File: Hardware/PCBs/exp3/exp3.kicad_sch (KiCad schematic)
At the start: 8 parts, among them J1 Conn_01x07_Female, J2 Conn_01x06_Female, U1 74HC86, U2 7483

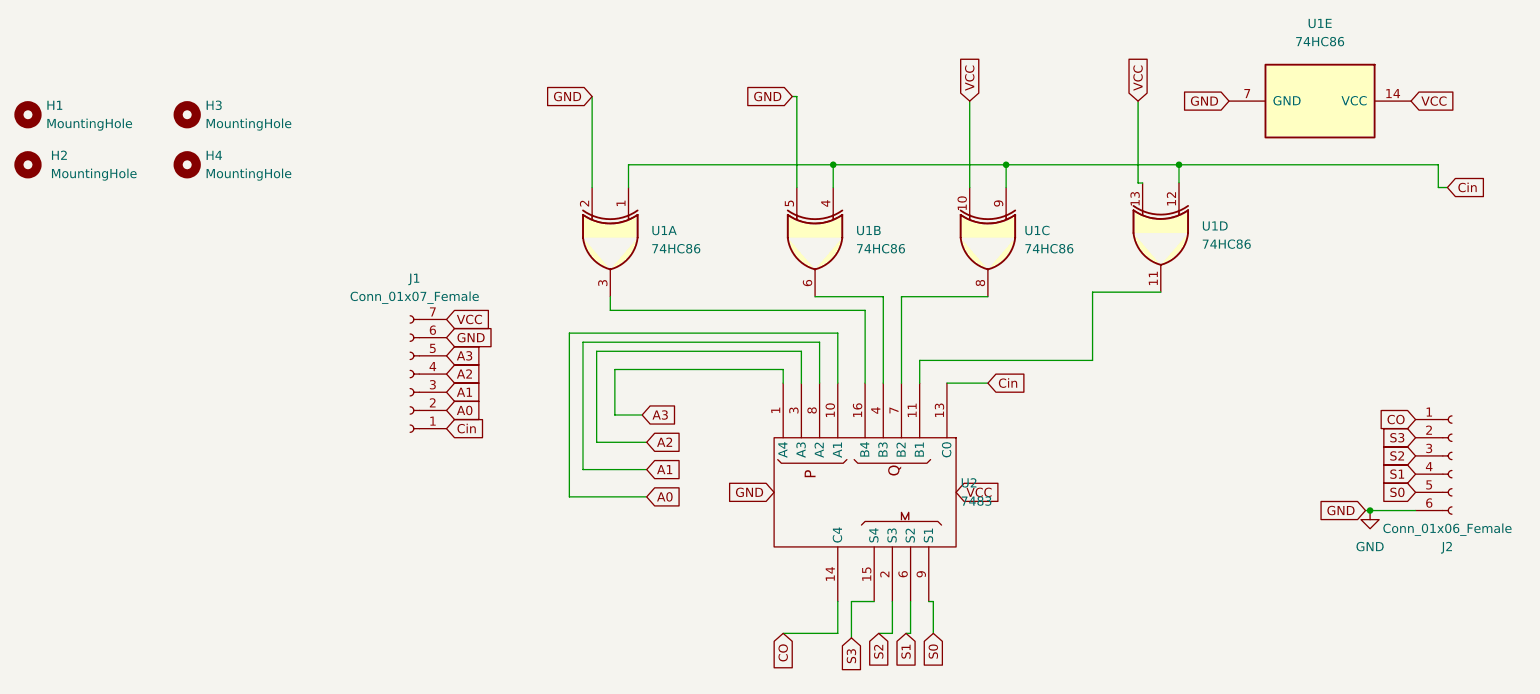
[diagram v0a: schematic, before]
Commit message: exp 3 PCB updated
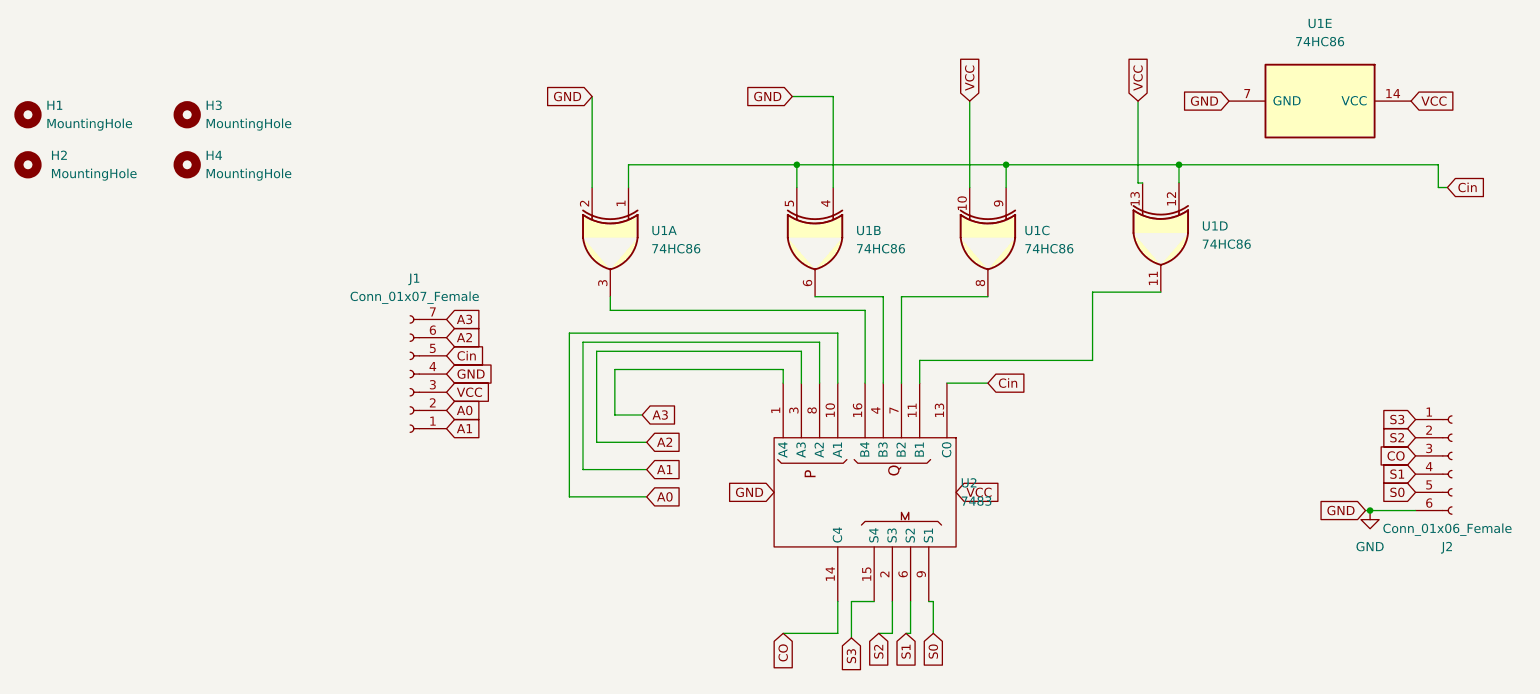
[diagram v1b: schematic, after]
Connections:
- net A1: now also J1.1 (Pin_1); no longer J1.3 (Pin_3)
- net A2: now also J1.6 (Pin_6); no longer J1.4 (Pin_4)
- net A3: now also J1.7 (Pin_7); no longer J1.5 (Pin_5)
- net CO: now also J2.3 (Pin_3); no longer J2.1 (Pin_1)
- net Cin: now also J1.5 (Pin_5), U1.5; no longer J1.1 (Pin_1), U1.4
- net GND: now also J1.4 (Pin_4), U1.4; no longer J1.6 (Pin_6), U1.5
- net S2: now also J2.2 (Pin_2); no longer J2.3 (Pin_3)
- net S3: now also J2.1 (Pin_1); no longer J2.2 (Pin_2)
- net VCC: now also J1.3 (Pin_3); no longer J1.7 (Pin_7)
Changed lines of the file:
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@@
   (junction (at 206.375 50.165) (diameter 0) (color 0 0 0 0)
   )
-  (junction (at 158.115 50.165) (diameter 0) (color 0 0 0 0)
+  (junction (at 153.035 50.165) (diameter 0) (color 0 0 0 0)
   )
   (junction (at 182.245 50.165) (diameter 0) (color 0 0 0 0)
@@
     (stroke (width 0) (type default) (color 0 0 0 0))
   )
-  (wire (pts (xy 158.115 50.165) (xy 158.115 53.34))
-    (stroke (width 0) (type default) (color 0 0 0 0))
-  )
   (wire (pts (xy 168.91 115.57) (xy 168.275 115.57))
     (stroke (width 0) (type default) (color 0 0 0 0))
   )
+  (wire (pts (xy 153.035 50.165) (xy 153.035 53.34))
+    (stroke (width 0) (type default) (color 0 0 0 0))
+  )
   (wire (pts (xy 233.045 98.425) (xy 239.395 98.425))
     (stroke (width 0) (type default) (color 0 0 0 0))
@@
     (stroke (width 0) (type default) (color 0 0 0 0))
   )
+  (wire (pts (xy 153.035 50.165) (xy 182.245 50.165))
+    (stroke (width 0) (type default) (color 0 0 0 0))
+  )
   (wire (pts (xy 123.19 74.93) (xy 156.21 74.93))
     (stroke (width 0) (type default) (color 0 0 0 0))
   )
-  (wire (pts (xy 153.035 40.64) (xy 153.035 53.34))
-    (stroke (width 0) (type default) (color 0 0 0 0))
-  )
   (wire (pts (xy 153.67 76.2) (xy 153.67 80.645))
     (stroke (width 0) (type default) (color 0 0 0 0))
@@
     (stroke (width 0) (type default) (color 0 0 0 0))
   )
-  (wire (pts (xy 158.115 50.165) (xy 182.245 50.165))
+  (wire (pts (xy 129.54 50.165) (xy 153.035 50.165))
     (stroke (width 0) (type default) (color 0 0 0 0))
   )
@@
     (stroke (width 0) (type default) (color 0 0 0 0))
   )
+  (wire (pts (xy 158.115 40.64) (xy 158.115 53.34))
+    (stroke (width 0) (type default) (color 0 0 0 0))
+  )
   (wire (pts (xy 129.54 53.34) (xy 129.54 50.165))
     (stroke (width 0) (type default) (color 0 0 0 0))
@@
     (stroke (width 0) (type default) (color 0 0 0 0))
   )
-  (wire (pts (xy 129.54 50.165) (xy 158.115 50.165))
-    (stroke (width 0) (type default) (color 0 0 0 0))
-  )
   (wire (pts (xy 172.085 111.125) (xy 172.085 115.57))
     (stroke (width 0) (type default) (color 0 0 0 0))
@@
     (stroke (width 0) (type default) (color 0 0 0 0))
   )
-  (wire (pts (xy 153.035 40.64) (xy 152.4 40.64))
+  (wire (pts (xy 152.4 40.64) (xy 158.115 40.64))
     (stroke (width 0) (type default) (color 0 0 0 0))
   )
@@
     (stroke (width 0) (type default) (color 0 0 0 0))
   )
-  (global_label "A2" (shape input) (at 104.14 79.375 0) (fields_autoplaced)
-    (effects (font (size 1.27 1.27)) (justify left))
-    (property "Intersheet References" "${INTERSHEET_REFS}" (id 0) (at 108.8512 79.4544 0)
-      (effects (font (size 1.27 1.27)) (justify left) hide)
-    )
-  )
   (global_label "VCC" (shape input) (at 200.66 41.275 90) (fields_autoplaced)
     (effects (font (size 1.27 1.27)) (justify left))
@@
     )
   )
-  (global_label "S2" (shape input) (at 239.395 90.805 180) (fields_autoplaced)
-    (effects (font (size 1.27 1.27)) (justify right))
-    (property "Intersheet References" "${INTERSHEET_REFS}" (id 0) (at 234.5629 90.7256 0)
-      (effects (font (size 1.27 1.27)) (justify right) hide)
-    )
-  )
   (global_label "VCC" (shape input) (at 177.165 41.275 90) (fields_autoplaced)
     (effects (font (size 1.27 1.27)) (justify left))
@@
     )
   )
-  (global_label "CO" (shape input) (at 239.395 85.725 180) (fields_autoplaced)
-    (effects (font (size 1.27 1.27)) (justify right))
-    (property "Intersheet References" "${INTERSHEET_REFS}" (id 0) (at 234.3814 85.6456 0)
-      (effects (font (size 1.27 1.27)) (justify right) hide)
-    )
-  )
-  (global_label "S3" (shape input) (at 239.395 88.265 180) (fields_autoplaced)
+  (global_label "GND" (shape input) (at 104.14 79.375 0) (fields_autoplaced)
+    (effects (font (size 1.27 1.27)) (justify left))
+    (property "Intersheet References" "${INTERSHEET_REFS}" (id 0) (at 110.4236 79.2956 0)
+      (effects (font (size 1.27 1.27)) (justify left) hide)
+    )
+  )
+  (global_label "VCC" (shape input) (at 238.76 41.275 0) (fields_autoplaced)
+    (effects (font (size 1.27 1.27)) (justify left))
+    (property "Intersheet References" "${INTERSHEET_REFS}" (id 0) (at 244.8017 41.1956 0)
+      (effects (font (size 1.27 1.27)) (justify left) hide)
+    )
+  )
+  (global_label "A3" (shape input) (at 131.445 85.09 0) (fields_autoplaced)
+    (effects (font (size 1.27 1.27)) (justify left))
+    (property "Intersheet References" "${INTERSHEET_REFS}" (id 0) (at 136.1562 85.1694 0)
+      (effects (font (size 1.27 1.27)) (justify left) hide)
+    )
+  )
+  (global_label "A2" (shape input) (at 104.14 74.295 0) (fields_autoplaced)
+    (effects (font (size 1.27 1.27)) (justify left))
+    (property "Intersheet References" "${INTERSHEET_REFS}" (id 0) (at 108.8512 74.3744 0)
+      (effects (font (size 1.27 1.27)) (justify left) hide)
+    )
+  )
+  (global_label "S2" (shape input) (at 239.395 88.265 180) (fields_autoplaced)
     (effects (font (size 1.27 1.27)) (justify right))
     (property "Intersheet References" "${INTERSHEET_REFS}" (id 0) (at 234.5629 88.1856 0)
@@
     )
   )
-  (global_label "VCC" (shape input) (at 238.76 41.275 0) (fields_autoplaced)
-    (effects (font (size 1.27 1.27)) (justify left))
-    (property "Intersheet References" "${INTERSHEET_REFS}" (id 0) (at 244.8017 41.1956 0)
-      (effects (font (size 1.27 1.27)) (justify left) hide)
-    )
-  )
-  (global_label "A3" (shape input) (at 131.445 85.09 0) (fields_autoplaced)
-    (effects (font (size 1.27 1.27)) (justify left))
-    (property "Intersheet References" "${INTERSHEET_REFS}" (id 0) (at 136.1562 85.1694 0)
-      (effects (font (size 1.27 1.27)) (justify left) hide)
-    )
-  )
   (global_label "GND" (shape input) (at 149.86 95.885 180) (fields_autoplaced)
     (effects (font (size 1.27 1.27)) (justify right))
@@
     )
   )
-  (global_label "A3" (shape input) (at 104.14 76.835 0) (fields_autoplaced)
-    (effects (font (size 1.27 1.27)) (justify left))
-    (property "Intersheet References" "${INTERSHEET_REFS}" (id 0) (at 108.8512 76.9144 0)
+  (global_label "VCC" (shape input) (at 104.14 81.915 0) (fields_autoplaced)
+    (effects (font (size 1.27 1.27)) (justify left))
+    (property "Intersheet References" "${INTERSHEET_REFS}" (id 0) (at 110.1817 81.8356 0)
+      (effects (font (size 1.27 1.27)) (justify left) hide)
+    )
+  )
+  (global_label "S3" (shape input) (at 239.395 85.725 180) (fields_autoplaced)
+    (effects (font (size 1.27 1.27)) (justify right))
+    (property "Intersheet References" "${INTERSHEET_REFS}" (id 0) (at 234.5629 85.6456 0)
+      (effects (font (size 1.27 1.27)) (justify right) hide)
+    )
+  )
+  (global_label "A1" (shape input) (at 104.14 86.995 0) (fields_autoplaced)
+    (effects (font (size 1.27 1.27)) (justify left))
+    (property "Intersheet References" "${INTERSHEET_REFS}" (id 0) (at 108.8512 87.0744 0)
+      (effects (font (size 1.27 1.27)) (justify left) hide)
+    )
+  )
+  (global_label "A0" (shape input) (at 104.14 84.455 0) (fields_autoplaced)
+    (effects (font (size 1.27 1.27)) (justify left))
+    (property "Intersheet References" "${INTERSHEET_REFS}" (id 0) (at 108.8512 84.5344 0)
       (effects (font (size 1.27 1.27)) (justify left) hide)
     )
@@
     )
   )
-  (global_label "Cin" (shape input) (at 104.14 86.995 0) (fields_autoplaced)
-    (effects (font (size 1.27 1.27)) (justify left))
-    (property "Intersheet References" "${INTERSHEET_REFS}" (id 0) (at 109.5769 86.9156 0)
-      (effects (font (size 1.27 1.27)) (justify left) hide)
-    )
-  )
   (global_label "Cin" (shape input) (at 179.705 80.645 0) (fields_autoplaced)
     (effects (font (size 1.27 1.27)) (justify left))
@@
     )
   )
-  (global_label "GND" (shape input) (at 104.14 74.295 0) (fields_autoplaced)
-    (effects (font (size 1.27 1.27)) (justify left))
-    (property "Intersheet References" "${INTERSHEET_REFS}" (id 0) (at 110.4236 74.2156 0)
-      (effects (font (size 1.27 1.27)) (justify left) hide)
-    )
-  )
   (global_label "A1" (shape input) (at 132.08 92.71 0) (fields_autoplaced)
     (effects (font (size 1.27 1.27)) (justify left))
@@
     )
   )
-  (global_label "VCC" (shape input) (at 104.14 71.755 0) (fields_autoplaced)
-    (effects (font (size 1.27 1.27)) (justify left))
-    (property "Intersheet References" "${INTERSHEET_REFS}" (id 0) (at 110.1817 71.6756 0)
-      (effects (font (size 1.27 1.27)) (justify left) hide)
-    )
-  )
   (global_label "S1" (shape input) (at 239.395 93.345 180) (fields_autoplaced)
     (effects (font (size 1.27 1.27)) (justify right))
@@
     )
   )
-  (global_label "A1" (shape input) (at 104.14 81.915 0) (fields_autoplaced)
-    (effects (font (size 1.27 1.27)) (justify left))
-    (property "Intersheet References" "${INTERSHEET_REFS}" (id 0) (at 108.8512 81.9944 0)
+  (global_label "Cin" (shape input) (at 104.14 76.835 0) (fields_autoplaced)
+    (effects (font (size 1.27 1.27)) (justify left))
+    (property "Intersheet References" "${INTERSHEET_REFS}" (id 0) (at 109.5769 76.7556 0)
       (effects (font (size 1.27 1.27)) (justify left) hide)
     )
@@
     )
   )
-  (global_label "A0" (shape input) (at 104.14 84.455 0) (fields_autoplaced)
-    (effects (font (size 1.27 1.27)) (justify left))
-    (property "Intersheet References" "${INTERSHEET_REFS}" (id 0) (at 108.8512 84.5344 0)
+  (global_label "A3" (shape input) (at 104.14 71.755 0) (fields_autoplaced)
+    (effects (font (size 1.27 1.27)) (justify left))
+    (property "Intersheet References" "${INTERSHEET_REFS}" (id 0) (at 108.8512 71.8344 0)
       (effects (font (size 1.27 1.27)) (justify left) hide)
     )
@@
     )
   )
+  (global_label "CO" (shape input) (at 239.395 90.805 180) (fields_autoplaced)
+    (effects (font (size 1.27 1.27)) (justify right))
+    (property "Intersheet References" "${INTERSHEET_REFS}" (id 0) (at 234.3814 90.7256 0)
+      (effects (font (size 1.27 1.27)) (justify right) hide)
+    )
+  )
